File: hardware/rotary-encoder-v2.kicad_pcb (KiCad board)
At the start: 2 copper layers, 30 x 25 mm, 25 parts, among them P1 CON-SENSOR2, P2 BOOT, P3 DEBUG, U1 XMC110024, U2 ROTARY_ENCODER, U3 DRILL, U4 DRILL, U5 DRILL, U6 DRILL

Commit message: Change capacitor footprint(s) to C0402F
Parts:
- C4: footprint kicad-libraries:C0402E -> kicad-libraries:C0402F
- D1: footprint kicad-libraries:D0603E -> kicad-libraries:D0603F
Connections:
- P1 pad 1: (no net) -> Net-(P1-Pad1)
- RP2 pad 2: (no net) -> Net-(RP2-Pad2)
- U1 pad 11: (no net) -> Net-(U1-Pad11)
- U1 pad 12: (no net) -> Net-(U1-Pad12)
- U1 pad 13: (no net) -> Net-(U1-Pad13)
- U1 pad 14: (no net) -> Net-(U1-Pad14)
- U1 pad 17: (no net) -> Net-(U1-Pad17)
- U1 pad 18: (no net) -> Net-(U1-Pad18)
- U1 pad 19: (no net) -> Net-(U1-Pad19)
- U1 pad 20: (no net) -> Net-(U1-Pad20)
- U1 pad 21: (no net) -> Net-(U1-Pad21)
- U1 pad 4: (no net) -> Net-(U1-Pad4)
- U1 pad 6: (no net) -> Net-(U1-Pad6)
- U1 pad 8: (no net) -> Net-(U1-Pad8)

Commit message: drc, fix status text
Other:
- board text added: "Status"
- board text removed: "status"

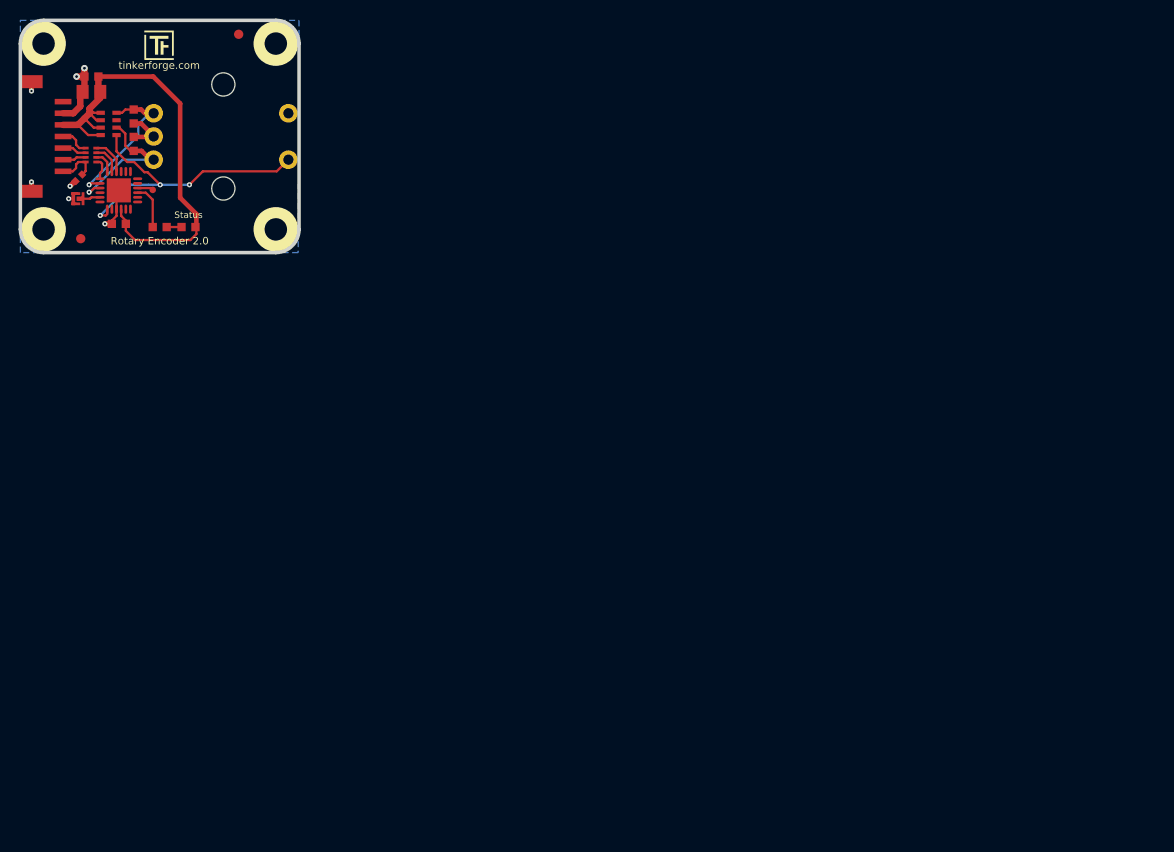
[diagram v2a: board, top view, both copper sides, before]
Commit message: New standart layout. Switched to Kicad 6
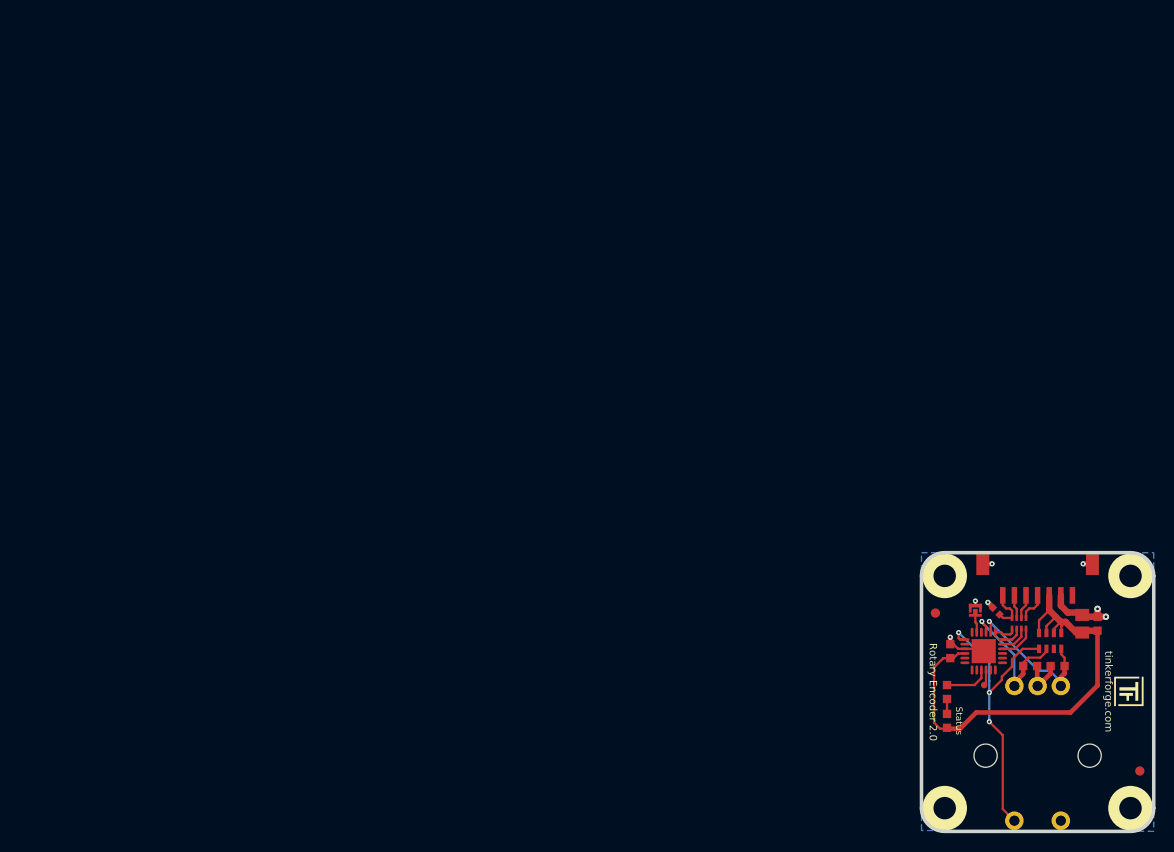
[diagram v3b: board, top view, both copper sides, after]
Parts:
- moved U6 130.3 mm to (162.4, 89.6), turned to -90 degrees
- moved G*** 128.1 mm to (163.8, 100.5), turned to -90 degrees
- moved Fiducial_Mark 125.3 mm to (163.4, 110.6), turned to -90 degrees
- moved U3 123.4 mm to (162.4, 114.6), turned to -90 degrees
- moved C2 123.3 mm to (158.8, 94.8), turned to 90 degrees
- moved C1 121.0 mm to (157.2, 94.8), turned to 90 degrees
- moved P1 118.3 mm to (152.4, 87.1), turned to 180 degrees
- moved C6 115.7 mm to (154.6, 99.3), turned to 180 degrees
- moved RP2 115.6 mm to (153.8, 96.6), turned to 180 degrees
- moved VAL 115.5 mm to (152.4, 92.5), turned to 90 degrees
- moved RP1 111.9 mm to (150.4, 94.7), turned to 180 degrees
- moved C5 111.7 mm to (151.6, 99.3), turned to 0 degrees
- moved VAL 110.8 mm to (152.4, 105.7), turned to 90 degrees
- moved U2 110.1 mm to (152.4, 109.0), turned to 90 degrees
- moved G*** 109.6 mm to (152.4, 112.0), turned to 90 degrees
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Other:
- board size 30 x 25 mm -> 25 x 30 mm
- net class Default removed

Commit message: Data Cleanup
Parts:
- moved U2 0.15 mm to (152.4, 108.8)
- moved P3 0.07 mm to (146.7, 101.4)
- moved C2 0.07 mm to (158.8, 94.8)
- moved C4 0.05 mm to (148.0, 93.4)
- moved C6 0.05 mm to (154.5, 99.3)
- moved RP2 0.05 mm to (153.8, 96.6)
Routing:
- net IN_A: track 17.7 -> 16.1 mm
- net IN_B: track 16.7 -> 15.6 mm
- net GND: track 27.2 -> 26.2 mm
- net VCC: track 51.4 -> 50.5 mm
